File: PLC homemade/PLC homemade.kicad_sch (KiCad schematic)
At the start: 0 parts

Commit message: :tada: completed power side of the schematic
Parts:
- added C1: 220uF 10V, symbol Device:C_Polarized
- added C2: 100nF 50V, symbol Device:C
- added C3: 10uF 50V, symbol Device:C
- added C4, C5, C6: 100uF 35V, symbol Device:C_Polarized_US
- added D1: SB1045L_C908747, SB1045L:TO-277_3P-L5.4-W4.0-LS6.5-TR, symbol SB1045L:SB1045L_C908747
- added D2: SS36, Diode_SMD:D_SMA, symbol Diode:SS36
- added D3: SFH460, Package_TO_SOT_THT:TO-18-2_Window, symbol LED:SFH460
- added L1: L, symbol Device:L
- added PS1: HLK-5M03, Converter_ACDC:Converter_ACDC_Hi-Link_HLK-5Mxx, symbol Converter_ACDC:HLK-5M03
- added R1: 1K, symbol Device:R
- added R2: 10K, symbol Device:R
- added R3: 10D-11, NTC10D-11:RES-TH_L12.5-W5.5-P7.50-D0.8-S5.50, symbol NTC10D-11:10D-11
- added U1: XC6220B331MR, Package_TO_SOT_SMD:SOT-23-5, symbol Regulator_Linear:XC6220B331MR
- added U2: XL1509-5.0E1, XL1509-5:SOIC-8_L5.0-W4.0-P1.27-LS6.0-BL, symbol XL1509-5.0E1:XL1509-5.0E1
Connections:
- new net: D1.1 (A), D1.3 (A), R3.1
- new net: C4.1, C5.1, C6.1
- new net: R2.2, U1.3 (CE)
- new net: D3.2 (A), R1.1
- new net 12V: D1.2 (K), PS1.4 (+Vout), R3.2, U2.1 (VIN)
- new net 3V3: C3.1, R1.2, U1.5 (VOUT)
- new net GND: C1.1, C2.2, C3.2, C4.2, C5.2, C6.2, D2.1 (K), D3.1 (K), PS1.3 (-Vout), U1.2 (GND), U2.4 (ON/OFF), U2.5 (GND), U2.6 (GND), U2.7 (GND), U2.8 (GND)
- new net LIVE: PS1.1 (AC/L)
- new net NEUTRAL: PS1.2 (AC/N)
- new net OUT5V: D2.2 (A), L1.1, U2.2 (OUTPUT)
- new net VCC: C1.2, C2.1, L1.2, R2.1, U1.1 (VIN), U2.3 (FB)

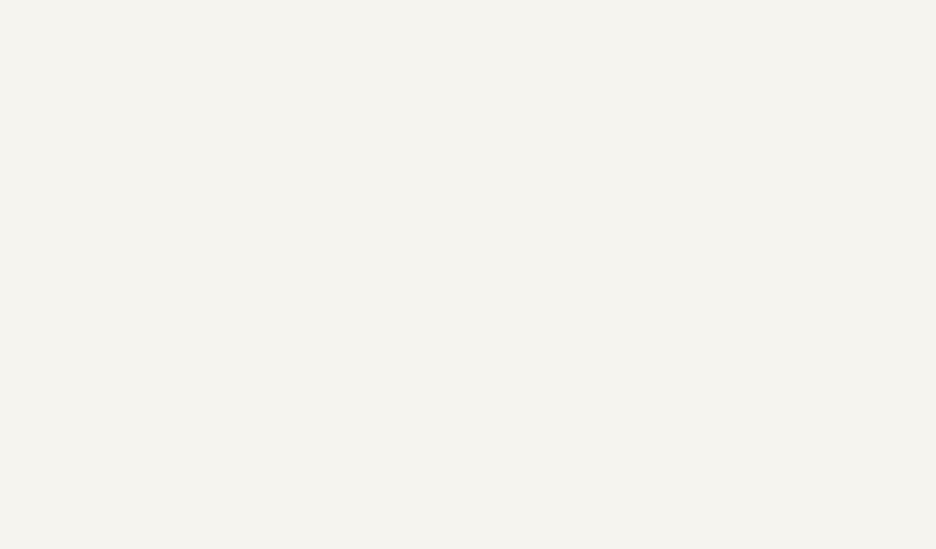
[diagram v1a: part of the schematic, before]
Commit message: :hammer: added ethernet page of the herachial sheet
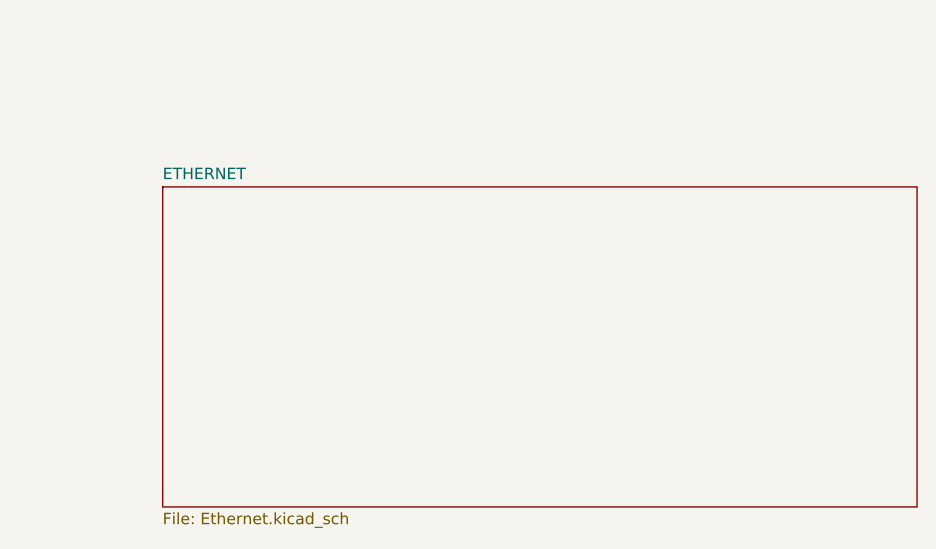
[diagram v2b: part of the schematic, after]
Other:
- added sheet ETHERNET (Ethernet.kicad_sch)
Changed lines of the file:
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@@
+		)
+	)
+	(sheet
+		(at 195.58 128.27)
+		(size 83.82 35.56)
+		(exclude_from_sim no)
+		(in_bom yes)
+		(on_board yes)
+		(dnp no)
+		(fields_autoplaced yes)
+		(stroke
+			(width 0.1524)
+			(type solid)
+		)
+		(fill
+			(color 0 0 0 0.0000)
+		)
+		(property "Sheetname" "ETHERNET"
+			(at 195.58 127.5584 0)
+			(effects
+				(font
+					(size 1.27 1.27)
+				)
+				(justify left bottom)
+			)
+		)
+		(property "Sheetfile" "Ethernet.kicad_sch"
+			(at 195.58 164.4146 0)
+			(effects
+				(font
+					(size 1.27 1.27)
+				)
+				(justify left top)
+			)
+		)
+		(instances
+			(project "PLC homemade"
+				(path "/152f83be-52d6-49bf-8437-949cb175c923"
+					(page "2")
+				)
+			)
 		)
 	)

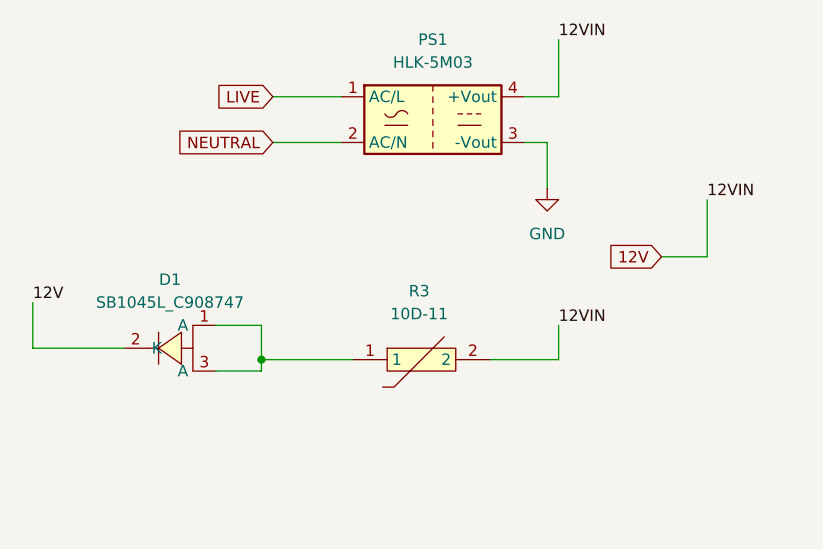
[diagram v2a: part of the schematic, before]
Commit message: :chart_with_upwards_trend:COMPLETED EHERNET, left 1 component out
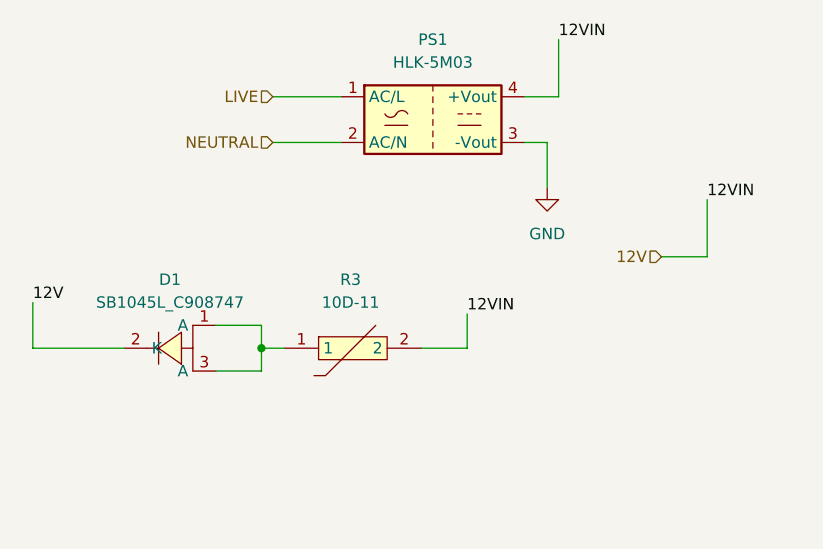
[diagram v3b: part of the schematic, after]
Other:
- moved on the sheet: R3
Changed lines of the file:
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@@
+	)
+	(junction
+		(at 59.69 74.93)
+		(diameter 0)
+		(color 0 0 0 0)
 	)
 	(junction
@@
 	)
 	(junction
-		(at 59.69 76.2)
-		(diameter 0)
-		(color 0 0 0 0)
-	)
-	(junction
 		(at 123.19 139.7)
 		(diameter 0)
@@
 	(wire
 		(pts
-			(xy 69.85 76.2) (xy 59.69 76.2)
+			(xy 62.23 74.93) (xy 59.69 74.93)
 		)
 		(stroke
@@
 	(wire
 		(pts
-			(xy 85.09 76.2) (xy 92.71 76.2)
+			(xy 77.47 74.93) (xy 82.55 74.93)
 		)
 		(stroke
@@
 	(wire
 		(pts
-			(xy 59.69 77.47) (xy 59.69 76.2)
+			(xy 59.69 74.93) (xy 59.69 77.47)
 		)
 		(stroke
@@
 	(wire
 		(pts
-			(xy 59.69 76.2) (xy 59.69 72.39)
-		)
-		(stroke
-			(width 0)
-			(type default)
-		)
-	)
-	(wire
-		(pts
 			(xy 60.96 46.99) (xy 68.58 46.99)
 		)
@@
 	(wire
 		(pts
-			(xy 92.71 76.2) (xy 92.71 72.39)
+			(xy 82.55 74.93) (xy 82.55 71.12)
 		)
 		(stroke
@@
 		(pts
 			(xy 63.5 139.7) (xy 63.5 144.78)
+		)
+		(stroke
+			(width 0)
+			(type default)
+		)
+	)
+	(wire
+		(pts
+			(xy 59.69 74.93) (xy 59.69 72.39)
 		)
 		(stroke
@@
 	)
 	(label "12VIN"
-		(at 92.71 72.39 0)
-		(effects
-			(font
-				(size 1.27 1.27)
-			)
-			(justify left bottom)
-		)
-	)
-	(label "12VIN"
 		(at 92.71 40.64 0)
 		(effects
@@
 		)
 	)
-	(global_label "LIVE"
-		(shape input)
-		(at 60.96 46.99 180)
-		(fields_autoplaced yes)
+	(label "12VIN"
+		(at 82.55 71.12 0)
 		(effects
 			(font
 				(size 1.27 1.27)
 			)
-			(justify right)
-		)
-		(property "Intersheetrefs" "${INTERSHEET_REFS}"
-			(at 54.1043 46.99 0)
-			(effects
-				(font
-					(size 1.27 1.27)
-				)
-				(justify right)
-				(hide yes)
-			)
-		)
-	)
-	(global_label "NEUTRAL"
+			(justify left bottom)
+		)
+	)
+	(hierarchical_label "NEUTRAL"
 		(shape input)
 		(at 60.96 52.07 180)
-		(fields_autoplaced yes)
 		(effects
 			(font
@@
 			(justify right)
 		)
-		(property "Intersheetrefs" "${INTERSHEET_REFS}"
-			(at 49.8105 52.07 0)
-			(effects
-				(font
-					(size 1.27 1.27)
-				)
-				(justify right)
-				(hide yes)
-			)
-		)
-	)
-	(global_label "12V"
+	)
+	(hierarchical_label "LIVE"
 		(shape input)
-		(at 104.14 64.77 180)
-		(fields_autoplaced yes)
+		(at 60.96 46.99 180)
 		(effects
 			(font
@@
 			(justify right)
 		)
-		(property "Intersheetrefs" "${INTERSHEET_REFS}"
-			(at 97.6472 64.77 0)
-			(effects
-				(font
-					(size 1.27 1.27)
-				)
-				(justify right)
-				(hide yes)
-			)
+	)
+	(hierarchical_label "12V"
+		(shape input)
+		(at 104.14 64.77 180)
+		(effects
+			(font
+				(size 1.27 1.27)
+			)
+			(justify right)
 		)
 	)
@@
 	(symbol
 		(lib_id "NTC10D-11:10D-11")
-		(at 77.47 76.2 0)
+		(at 69.85 74.93 0)
 		(unit 1)
 		(exclude_from_sim no)
@@
 		(fields_autoplaced yes)
 		(property "Reference" "R3"
-			(at 77.215 68.58 0)
+			(at 69.595 67.31 0)
 			(effects
 				(font
@@
 		)
 		(property "Value" "10D-11"
-			(at 77.215 71.12 0)
+			(at 69.595 69.85 0)
 			(effects
 				(font
@@
 		)
 		(property "Footprint" "NTC10D-11:RES-TH_L12.5-W5.5-P7.50-D0.8-S5.50"
-			(at 77.47 83.82 0)
+			(at 69.85 82.55 0)
 			(effects
 				(font
@@
 		)
 		(property "Datasheet" "https://lcsc.com/product-detail/NTC-Thermistors_NTCThermistor10R_C53820.html"
-			(at 77.47 86.36 0)
+			(at 69.85 85.09 0)
 			(effects
 				(font
@@
 		)
 		(property "Description" ""
-			(at 77.47 76.2 0)
+			(at 69.85 74.93 0)
 			(effects
 				(font
@@
 		)
 		(property "LCSC Part" "C53820"
-			(at 77.47 88.9 0)
-			(effects
-				(font
+			(at 69.85 87.63 0)
+			(effects
+				(font

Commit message: :green_heart: CoRRECTED pOWER eRRORS
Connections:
- net 12V: now also C4.1, C5.1, C6.1
- net 3V3 renamed 3.3V

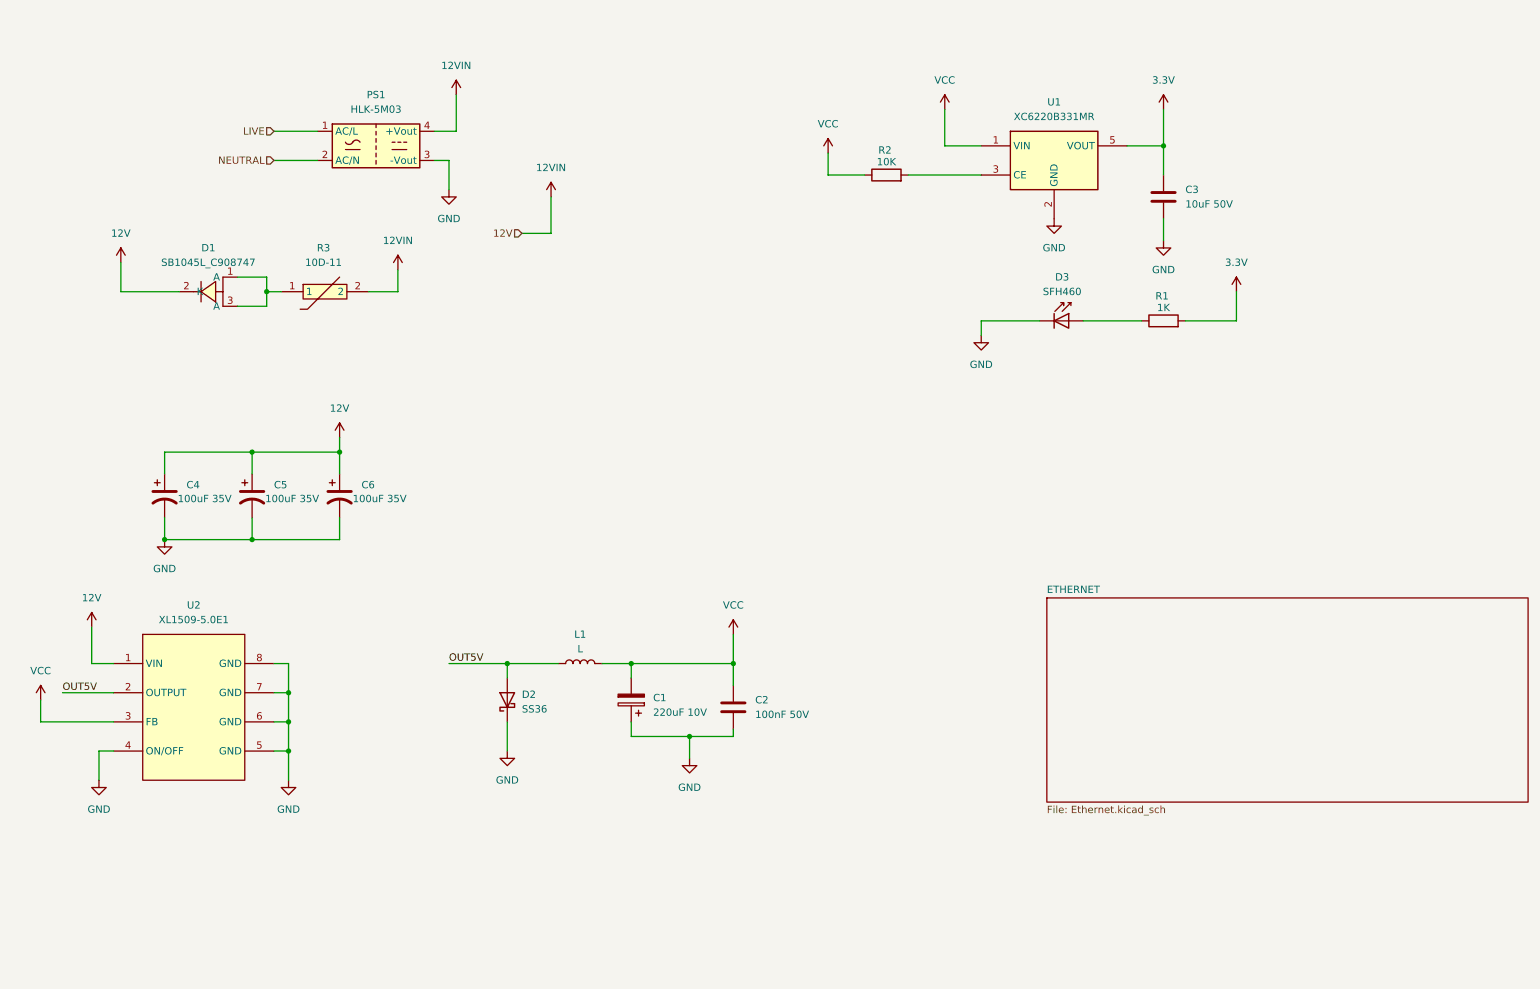
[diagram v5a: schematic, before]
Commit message: :art: grouped Power section
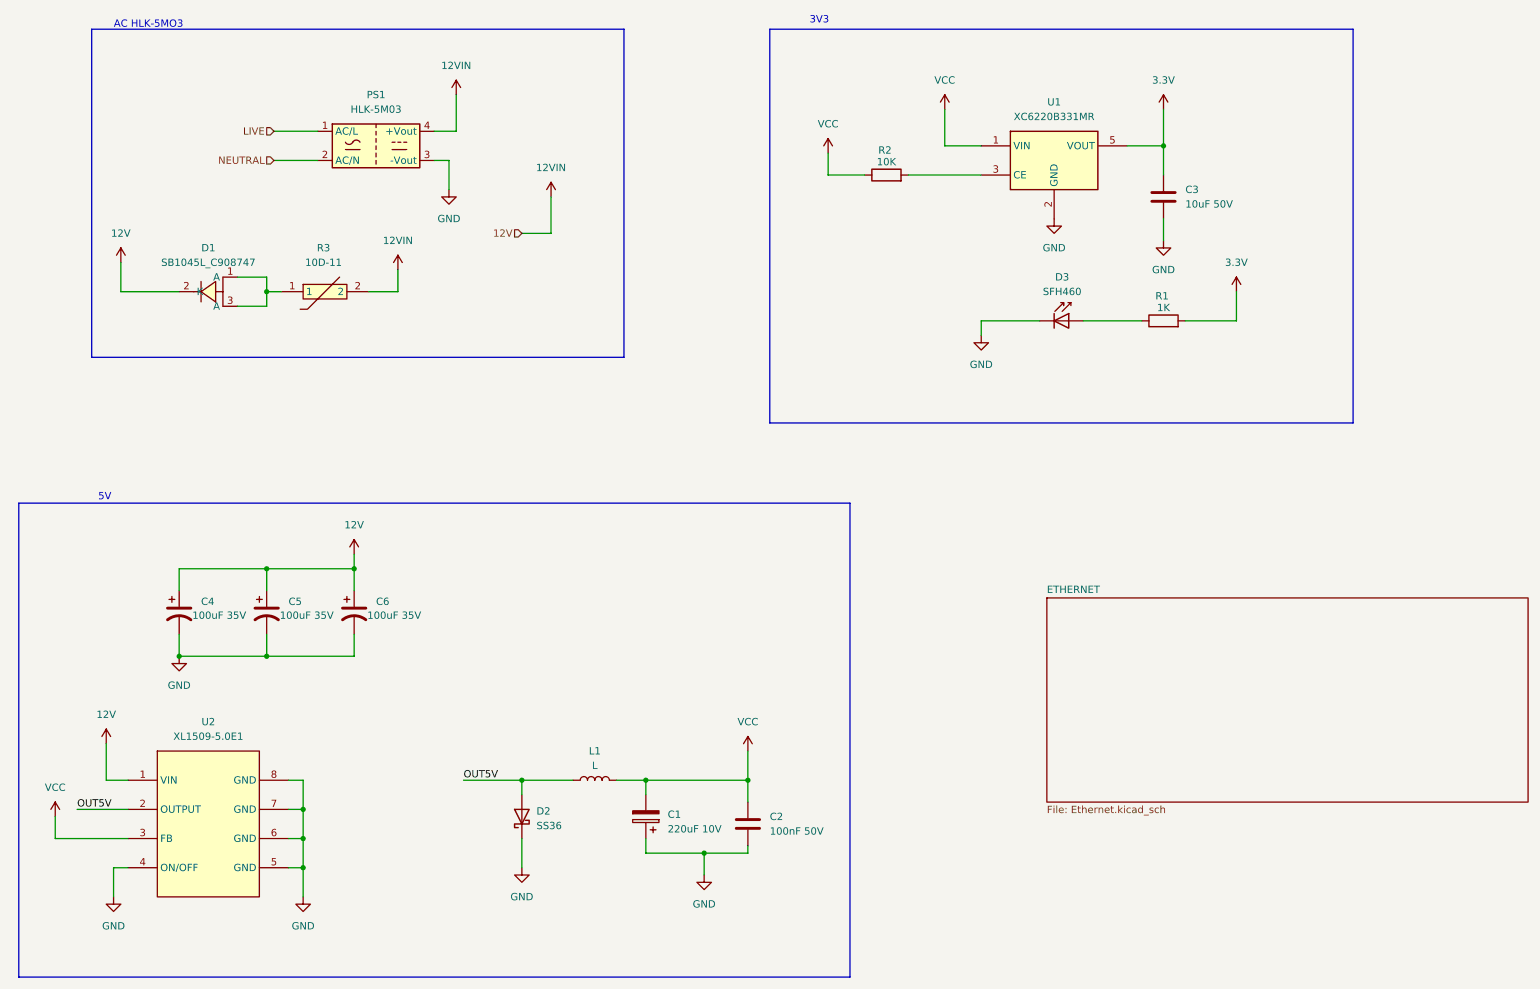
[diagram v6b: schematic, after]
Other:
- note added: "3V3"
- note added: "5V"
- note added: "AC HLK-5MO3"
- moved on the sheet: C1, C2, C4, C5, C6, D2, L1, U2

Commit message: :clown_face: changed HEIRACHIAL to global
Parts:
- added J14, J15: Conn_01x02, symbol Connector_Generic:Conn_01x02
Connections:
- net 12V: now also J15.1 (Pin_1)
- net GND: now also J15.2 (Pin_2)
- net LIVE: now also J14.1 (Pin_1)
- net NEUTRAL: now also J14.2 (Pin_2)

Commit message: :tada: Run Electrical rule checker All errors corrected
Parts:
- C1, C2, C4, C5, C6: footprint (none) -> Capacitor_SMD:C_0201_0603Metric
- C3: footprint (none) -> Capacitor_SMD:C_01005_0402Metric
- J14: footprint (none) -> Connector_Phoenix_MC:PhoenixContact_MCV_1,5_2-GF-3.81_1x02_P3.81mm_Vertical_ThreadedFlange
- J15: footprint (none) -> Connector_PinHeader_1.00mm:PinHeader_1x02_P1.00mm_Vertical_SMD_Pin1Left
- L1: footprint (none) -> Inductor_SMD:L_APV_APH1040
- R1: footprint (none) -> Crystal:Crystal_SMD_5032-2Pin_5.0x3.2mm
- R2: footprint (none) -> Resistor_SMD:R_01005_0402Metric
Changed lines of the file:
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@@
 			)
 		)
-		(property "Footprint" ""
+		(property "Footprint" "Inductor_SMD:L_APV_APH1040"
 			(at 116.84 160.02 0)
 			(effects
@@
 			)
 		)
-		(property "Footprint" ""
+		(property "Footprint" "Capacitor_SMD:C_0201_0603Metric"
 			(at 144.4752 171.45 0)
 			(effects
@@
 			)
 		)
-		(property "Footprint" ""
+		(property "Footprint" "Capacitor_SMD:C_0201_0603Metric"
 			(at 74.93 130.81 0)
 			(effects
@@
 			)
 		)
-		(property "Footprint" ""
+		(property "Footprint" "Capacitor_SMD:C_0201_0603Metric"
 			(at 124.7648 162.56 0)
 			(effects
@@
 			)
 		)
-		(property "Footprint" ""
+		(property "Footprint" "Resistor_SMD:R_01005_0402Metric"
 			(at 167.64 56.388 90)
 			(effects
@@
 			)
 		)
-		(property "Footprint" ""
+		(property "Footprint" "Capacitor_SMD:C_0201_0603Metric"
 			(at 59.69 130.81 0)
 			(effects
@@
 			)
 		)
-		(property "Footprint" ""
+		(property "Footprint" "Crystal:Crystal_SMD_5032-2Pin_5.0x3.2mm"
 			(at 215.9 81.788 90)
 			(effects
@@
 			)
 		)
-		(property "Footprint" ""
+		(property "Footprint" "Capacitor_SMD:C_01005_0402Metric"
 			(at 216.8652 62.23 0)
 			(effects
@@
 			)
 		)
-		(property "Footprint" ""
+		(property "Footprint" "Capacitor_SMD:C_0201_0603Metric"
 			(at 44.45 130.81 0)
 			(effects
@@
 			)
 		)
-		(property "Footprint" ""
+		(property "Footprint" "Connector_Phoenix_MC:PhoenixContact_MCV_1,5_2-GF-3.81_1x02_P3.81mm_Vertical_ThreadedFlange"
 			(at 49.53 35.56 0)
 			(effects
@@
 			)
 		)
-		(property "Footprint" ""
+		(property "Footprint" "Connector_PinHeader_1.00mm:PinHeader_1x02_P1.00mm_Vertical_SMD_Pin1Left"
 			(at 105.41 72.39 0)
 			(effects
